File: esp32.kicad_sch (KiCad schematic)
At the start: 28 parts, among them U1 ESP32-C3-WROOM-02, U10 74LVC1G08

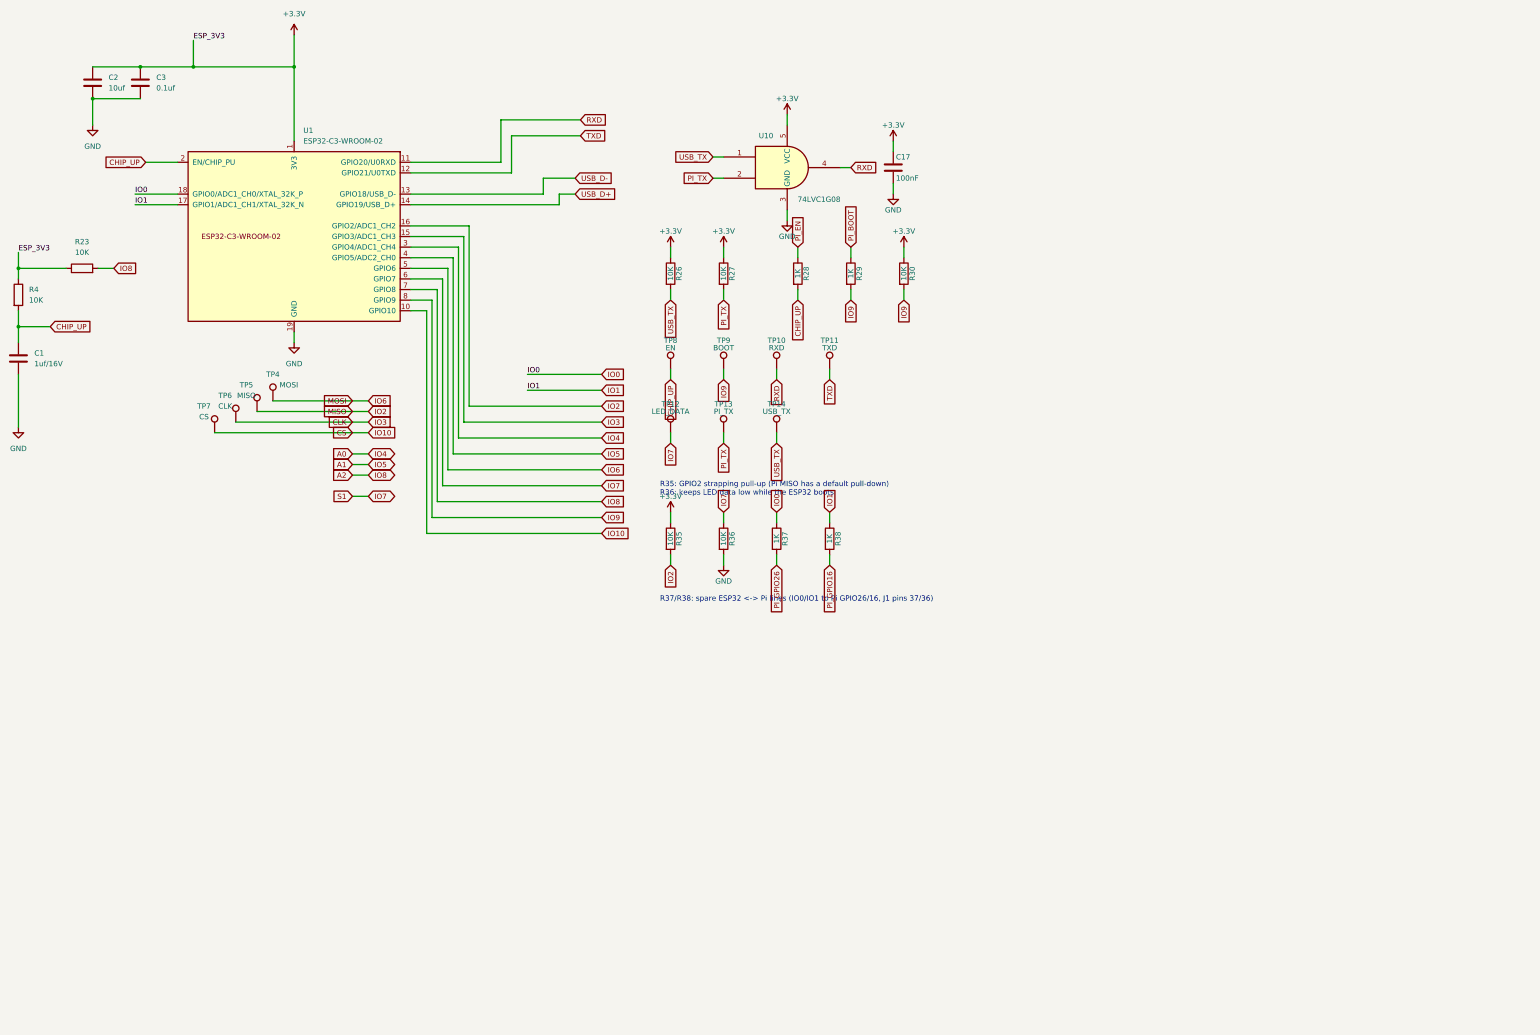
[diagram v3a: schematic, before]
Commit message: Test board schematic: bare ESP32-C3FH4, native USB, noise fixes
A - bare chip (docs/esp32-c3-chip-design.md):
- ESP32-C3FH4 (4 MB in-package flash) replaces the WROOM-02 module
- Espressif reference core: VDD3P3 2.0 nH filter + 1 uF, VDDA 1 uF + 10 nF,
  RTC/CPU 100 nF, VDD_SPI 1 uF, 40 MHz crystal with 24 nH series and 22 pF
- RF: CLC match at the chip, pi footprint with 6.8 nH at a Walsin
  RFANT3216120A5T chip antenna (shunts DNP for tuning)
- 499 ohm on U0TXD

B - native USB:
- USB-C D+/D- via ESD and 22 ohm to GPIO19/18 (USB Serial/JTAG);
  D+ pull-up footprint DNP
- CP2102N, DTR/RTS auto-reset and the UART AND gate removed; J1 pin 8
  drives ESP32 RX directly (R27 pull-up)

Noise fixes (docs/noise-analysis-v4.md):
- 10k pull-downs and SRV05-4 TVS arrays on CH1-CH8
- SMBJ5.0A TVS on +5V, 100 uF at J1, 3 x 100 nF spread on +5V

ERC: 0 errors. Board layout not updated yet.

Co-Authored-By: Claude Opus 5.5 <noreply@anthropic.com>
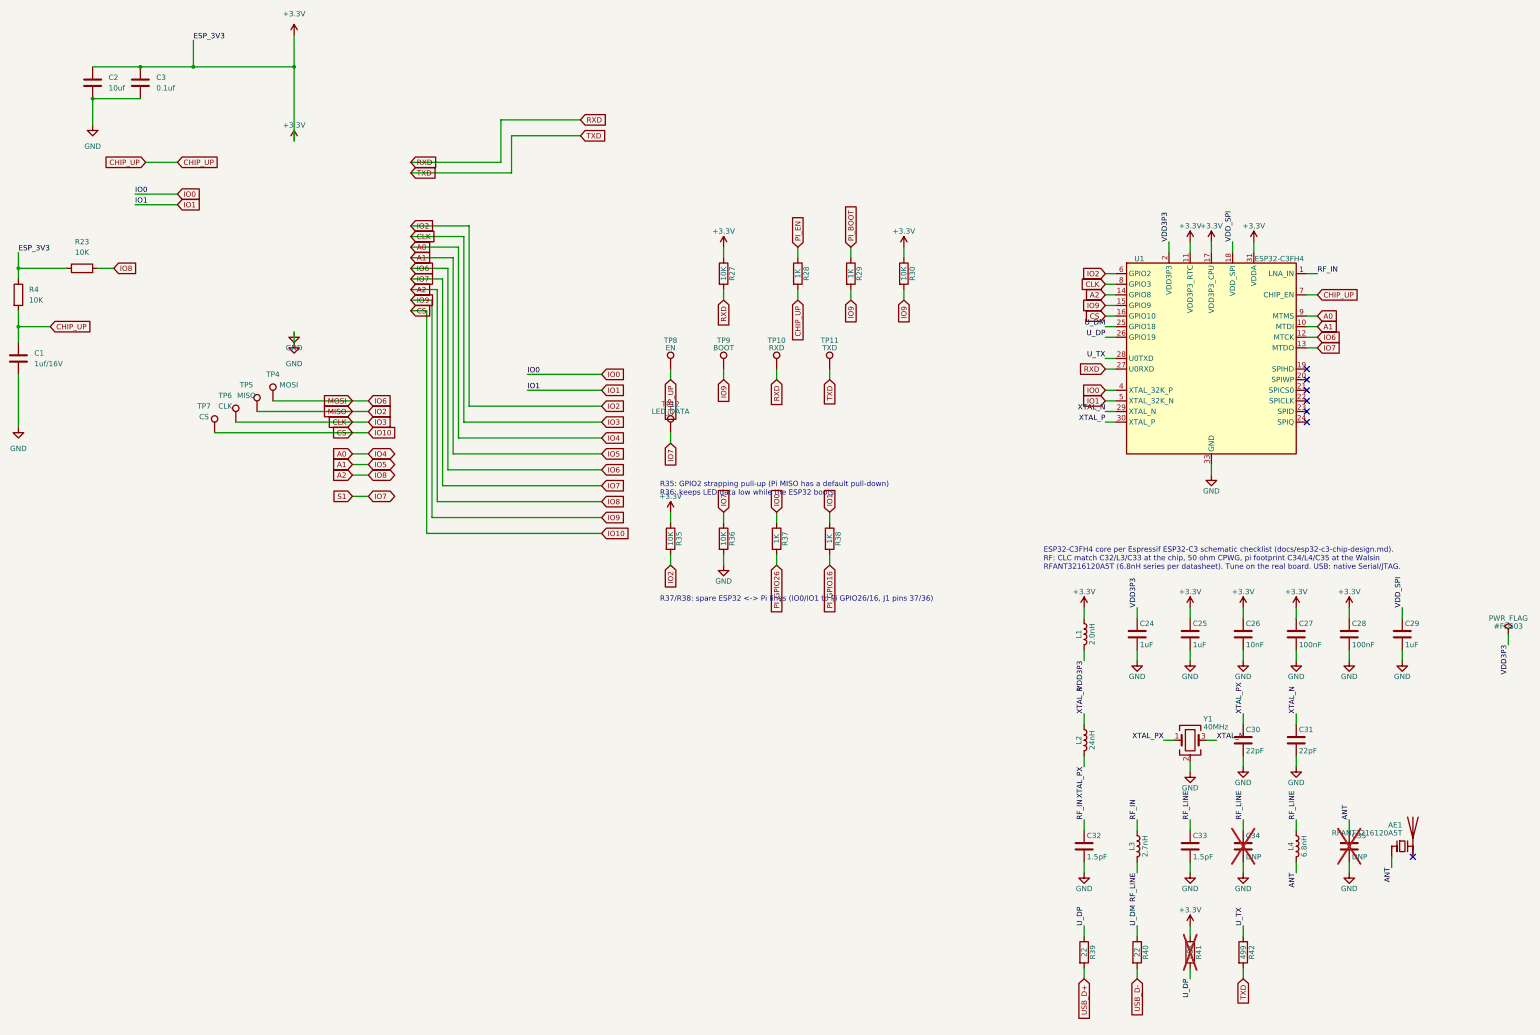
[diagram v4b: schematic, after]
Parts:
- removed C17: 100nF, Capacitor_SMD:C_0603_1608Metric, symbol Device:C
- removed R26: 10K, Resistor_SMD:R_0603_1608Metric, symbol Device:R
- removed TP13: PI_TX, TestPoint:TestPoint_Pad_1.0x1.0mm, symbol Connector:TestPoint
- removed TP14: USB_TX, TestPoint:TestPoint_Pad_1.0x1.0mm, symbol Connector:TestPoint
- removed U1: ESP32-C3-WROOM-02, PCM_Espressif:ESP32-C3-WROOM-02, symbol PCM_Espressif:ESP32-C3-WROOM-02
- removed U10: 74LVC1G08, Package_TO_SOT_SMD:SOT-353_SC-70-5, symbol 74xGxx:74LVC1G08
- added AE1: RFANT3216120A5T, Julelys:Walsin_RFANT3216120A5T, symbol Device:Antenna_Chip
- added C24, C25, C29: 1uF, Capacitor_SMD:C_0402_1005Metric, symbol Device:C
- added C26: 10nF, Capacitor_SMD:C_0402_1005Metric, symbol Device:C
- added C27, C28: 100nF, Capacitor_SMD:C_0402_1005Metric, symbol Device:C
- added C30, C31: 22pF, Capacitor_SMD:C_0402_1005Metric, symbol Device:C
- added C32, C33: 1.5pF, Capacitor_SMD:C_0402_1005Metric, symbol Device:C
- added C34, C35: DNP, Capacitor_SMD:C_0402_1005Metric, symbol Device:C
- added L1: 2.0nH, Inductor_SMD:L_0402_1005Metric, symbol Device:L
- added L2: 24nH, Inductor_SMD:L_0402_1005Metric, symbol Device:L
- added L3: 2.7nH, Inductor_SMD:L_0402_1005Metric, symbol Device:L
- added L4: 6.8nH, Inductor_SMD:L_0402_1005Metric, symbol Device:L
- added R39, R40: 22, Resistor_SMD:R_0402_1005Metric, symbol Device:R
- added R41: 1.5K, Resistor_SMD:R_0402_1005Metric, symbol Device:R
- added R42: 499, Resistor_SMD:R_0402_1005Metric, symbol Device:R
- added U1: ESP32-C3FH4, Package_DFN_QFN:QFN-32-1EP_5x5mm_P0.5mm_EP3.7x3.7mm, symbol MCU_Espressif:ESP32-C3
- added Y1: 40MHz, Crystal:Crystal_SMD_3225-4Pin_3.2x2.5mm, symbol Device:Crystal_GND24
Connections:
- net PI_TX is gone; now on net RXD: R27.2
- net +3.3V: now also C25.1, C26.1, C27.1, C28.1, L1.1, R41.1, U1.11 (VDD3P3_RTC), U1.17 (VDD3P3_CPU), U1.31 (VDDA), U1.32 (VDDA)
- net A0: now also U1.9 (MTMS)
- net A1: now also U1.10 (MTDI)
- net A2: now also U1.14 (GPIO8)
- net CHIP_UP: now also U1.7 (CHIP_EN)
- net CLK: now also U1.8 (GPIO3)
- net CS: now also U1.16 (GPIO10)
- net GND: now also C24.2, C25.2, C26.2, C27.2, C28.2, C29.2, C30.2, C31.2, C32.2, C33.2, C34.2, C35.2, U1.33 (GND), Y1.2 (G), Y1.4 (G)
- net IO0: now also U1.4 (XTAL_32K_P)
- net IO1: now also U1.5 (XTAL_32K_N)
- net IO2: now also U1.6 (GPIO2)
- net IO6: now also U1.12 (MTCK)
- net IO7: now also U1.13 (MTDO)
- net IO9: now also U1.15 (GPIO9)
- net RXD: now also U1.27 (U0RXD)
- net TXD: now also R42.2
- net USB_D+: now also R39.2
- net USB_D-: now also R40.2
- new net ANT: AE1.1 (FEED), C35.1, L4.2
- new net RF_IN: C32.1, L3.1, U1.1 (LNA_IN)
- new net RF_LINE: C33.1, C34.1, L3.2, L4.1
- new net U_DM: R40.1, U1.25 (GPIO18)
- new net U_DP: R39.1, R41.2, U1.26 (GPIO19)
- new net U_TX: R42.1, U1.28 (U0TXD)
- new net VDD3P3: C24.1, L1.2, U1.2 (VDD3P3), U1.3 (VDD3P3)
- new net VDD_SPI: C29.1, U1.18 (VDD_SPI)
- new net XTAL_N: C31.1, U1.29 (XTAL_N), Y1.3
- new net XTAL_P: L2.1, U1.30 (XTAL_P)
- new net XTAL_PX: C30.1, L2.2, Y1.1
- no-connect marks 0 -> 7
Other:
- note added: "ESP32-C3FH4 core per Espressif ESP32-C3 schematic checklist (docs/esp32-c3-chip-design.md). RF: CLC match C32/L3/C33 at the chip, 50 ohm CPWG, pi footprint C34/L4/C35 at the Walsin RFANT3216120A5T (6.8nH series per datasheet). Tune on the real board. USB: native Serial/JTAG."

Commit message: R42 -> 510R (C25123) and D4 -> B5819W (C8598), both JLC Basic parts
Saves two extended-part setup fees. Same footprints; JLC rotation and
polarity checked (CPL unchanged).

Co-Authored-By: Claude Opus 5.5 <noreply@anthropic.com>
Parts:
- R42: value 499 -> 510
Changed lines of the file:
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@@
       (effects (font (size 1.27 1.27)))
     )
-    (property "Value" "499" (at 337.82 251.46 90)
+    (property "Value" "510" (at 337.82 251.46 90)
       (effects (font (size 1.27 1.27)))
     )
